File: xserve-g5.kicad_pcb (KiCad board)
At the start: 2 copper layers, 100 x 50 mm, 4 parts, among them J1 SATA_Backplane_PWR, J2 FAN_LEFT, J3 FAN_RIGHT, J4 PWR

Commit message: update
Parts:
- added J10: FAN5_PWM, Connector_PinSocket_2.54mm:PinSocket_1x04_P2.54mm_Horizontal, F.Cu at (191.0, 107.5)
- added J11: FAN6_PWM, Connector_PinSocket_2.54mm:PinSocket_1x04_P2.54mm_Horizontal, F.Cu at (169.5, 107.5)
- added J12: FAN7_PWM, Connector_PinSocket_2.54mm:PinSocket_1x04_P2.54mm_Horizontal, F.Cu at (148.0, 107.5)
- added J5: PWR_R, Connector_TE-Connectivity:TE_MATE-N-LOK_350211-1_1x04_P5.08mm_Vertical, F.Cu at (217.0, 110.0)
- added J6: FAN1_PWM, Connector_PinSocket_2.54mm:PinSocket_1x04_P2.54mm_Horizontal, F.Cu at (133.0, 107.5)
- added J7: FAN2_PWM, Connector_PinSocket_2.54mm:PinSocket_1x04_P2.54mm_Horizontal, F.Cu at (111.5, 107.5)
- added J8: FAN3_PWM, Connector_PinSocket_2.54mm:PinSocket_1x04_P2.54mm_Horizontal, F.Cu at (90.0, 107.5)
- added J9: FAN4_PWM, Connector_PinSocket_2.54mm:PinSocket_1x04_P2.54mm_Horizontal, F.Cu at (68.5, 107.5)
- added JP1: PWM1_2, Connector_PinHeader_2.54mm:PinHeader_1x02_P2.54mm_Vertical, F.Cu at (125.0, 101.0)
- added JP2: PWM1_3, Connector_PinHeader_2.54mm:PinHeader_1x02_P2.54mm_Vertical, F.Cu at (104.0, 101.0)
- added JP3: PWM1_4, Connector_PinHeader_2.54mm:PinHeader_1x02_P2.54mm_Vertical, F.Cu at (82.0, 101.0)
- added JP4: PWM5_6, Connector_PinHeader_2.54mm:PinHeader_1x02_P2.54mm_Vertical, F.Cu at (183.0, 101.0)
- added JP5: PWM5_7, Connector_PinHeader_2.54mm:PinHeader_1x02_P2.54mm_Vertical, F.Cu at (161.5, 101.0)
- J4: value PWR -> PWR_L
- moved J3 68.3 mm to (228.5, 79.5), turned to 90 degrees
- moved J1 67.9 mm to (33.5, 92.5)
- moved J2 65.8 mm to (59.5, 66.5)
- moved J4 65.2 mm to (36.0, 110.5)
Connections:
- J1 pad 8: +3V3 -> Net-(J1-Pad8)
- J1 pad 9: +3V3 -> Net-(J1-Pad9)
- J2 pad 1: Net-(J2-Pad1) -> PWM1
- J2 pad 10: Net-(J2-Pad10) -> TACH4
- J2 pad 2: Net-(J2-Pad2) -> PWM2
- J2 pad 3: Net-(J2-Pad3) -> GND
- J2 pad 4: Net-(J2-Pad4) -> PWM3
- J2 pad 5: Net-(J2-Pad5) -> PWM4
- J2 pad 6: Net-(J2-Pad6) -> TACH1
- J2 pad 7: Net-(J2-Pad7) -> TACH2
- J2 pad 8: Net-(J2-Pad8) -> +12V
- J2 pad 9: Net-(J2-Pad9) -> TACH3
- J3 pad 1: Net-(J3-Pad1) -> PWM5
- J3 pad 10: Net-(J3-Pad10) -> +12V
- J3 pad 2: Net-(J3-Pad2) -> PWM6
- J3 pad 3: Net-(J3-Pad3) -> GND
- J3 pad 4: Net-(J3-Pad4) -> PWM7
- J3 pad 5: Net-(J3-Pad5) -> GND
- J3 pad 6: Net-(J3-Pad6) -> TACH5
- J3 pad 7: Net-(J3-Pad7) -> TACH6
- J3 pad 8: Net-(J3-Pad8) -> +12V
- J3 pad 9: Net-(J3-Pad9) -> TACH7
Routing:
- net PWM1: track 0.00 -> 163.8 mm
- net TACH1: track 0.00 -> 103.0 mm
- net TACH7: track 0.00 -> 99.4 mm
- net PWM7: track 0.00 -> 88.6 mm
- net PWM2: track 0.00 -> 86.9 mm
- net PWM5: track 0.00 -> 85.2 mm
- net +12V: track 24.0 -> 105.3 mm
- net TACH2: track 0.00 -> 79.9 mm
- net TACH6: track 0.00 -> 75.4 mm
- net PWM6: track 0.00 -> 64.6 mm
- net PWM3: track 0.00 -> 62.2 mm
- net TACH3: track 0.00 -> 54.6 mm
- net TACH5: track 0.00 -> 52.7 mm
- net PWM4: track 0.00 -> 44.3 mm
- net TACH4: track 0.00 -> 36.1 mm
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- added copper zone on B.Cu, net GND
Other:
- board size 100 x 50 mm -> 214 x 56.5 mm
- net class GND added: clearance 0.2, trace_width 1, via_dia 0.8, via_drill 0.4
- net class PWM added: clearance 0.2, trace_width 0.5, via_dia 0.8, via_drill 0.4
- net class TACH added: clearance 0.2, trace_width 0.5, via_dia 0.8, via_drill 0.4

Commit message: update
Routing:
- net PWM5: track 85.2 -> 91.4 mm
- net TACH5: track 52.7 -> 47.0 mm
- net PWM1: track 163.8 -> 159.2 mm
- net TACH1: track 103.0 -> 98.6 mm
- net TACH6: track 75.4 -> 71.3 mm
- net TACH2: track 79.9 -> 75.8 mm
- net TACH7: track 99.4 -> 95.5 mm
- net PWM3: track 62.2 -> 66.0 mm
- net TACH3: track 54.6 -> 51.8 mm
- net PWM2: track 86.9 -> 89.0 mm
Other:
- outline, holes or cut-outs redrawn
- net class Default: clearance 0.2 -> 0.3
- net class GND: clearance 0.2 -> 0.3
- net class PWM: clearance 0.2 -> 0.3
- net class TACH: clearance 0.2 -> 0.3
- rule trace_clearance: 0.2 -> 0.3

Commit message: updates
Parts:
- added J13: Front Panel, Connector_PinHeader_1.27mm:PinHeader_2x17_P1.27mm_Vertical, F.Cu at (85.0, 71.5)
- added U1: WeMos_D1_mini, Module:WEMOS_D1_mini_light, F.Cu at (173.5, 85.0)
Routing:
- net PWM3: track 66.0 -> 62.3 mm
- net PWM1: track 159.2 -> 161.9 mm
- net TACH1: track 98.6 -> 101.0 mm
- net TACH2: track 75.8 -> 77.7 mm
- net PWM2: track 89.0 -> 88.2 mm
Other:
- outline, holes or cut-outs redrawn
- net class Default: clearance 0.3 -> 0.25
- net class GND: clearance 0.3 -> 0.25
- rule trace_clearance: 0.3 -> 0.25

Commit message: update
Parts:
- added J14: SYSTEM_PINS, Connector_PinHeader_2.54mm:PinHeader_1x06_P2.54mm_Horizontal, F.Cu at (102.5, 75.0)
- added J15: CLED_VCC, Connector_PinHeader_2.54mm:PinHeader_1x03_P2.54mm_Vertical, F.Cu at (123.0, 67.0)
- moved J13 4.74 mm to (86.5, 67.0)
- moved U1 3.91 mm to (176.5, 87.5)
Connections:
- net Net-(J13-Pad22) renamed Q13
- J13 pad 14: Net-(J13-Pad14) -> CLED_SRCLR_n
- J13 pad 20: U6_?? -> CLED_SRCLR_n
- J13 pad 26: +5V -> +5VA
- J13 pad 28: +5V -> +5VA
- J13 pad 30: +5V -> +5VA
- J13 pad 32: +5V -> +5VA
- J13 pad 34: +5V -> +5VA
- J13 pad 4: CLED_VCC -> CLED_SRCLR_n
- J13 pad 9: Net-(J13-Pad9) -> CLED_SRCLR_n
- J3 pad 10: +12V -> +12VA
- J3 pad 8: +12V -> +12VA
- J5 pad 1: +12V -> +12VA
- U1 pad 4: Net-(U1-Pad4) -> CLED_SRCLK
- U1 pad 5: Net-(U1-Pad5) -> CLED_SER
- U1 pad 6: Net-(U1-Pad6) -> CLED_RCLK
- U1 pad 9: +5V -> +5VA
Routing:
- net CLED_SRCLK: track 0.00 -> 110.2 mm, vias 0 -> 2
- net CLED_RCLK: track 0.00 -> 110.2 mm
- net CLED_SER: track 0.00 -> 105.8 mm
- net +5VA: track 0.00 -> 97.6 mm, vias 0 -> 2
- net +3V3: track 0.00 -> 87.5 mm, vias 0 -> 2
- net +12VA: track 0.00 -> 55.4 mm
- net +12V: track 104.9 -> 49.4 mm
- net CLED_SRCLR_n: track 0.00 -> 45.6 mm
- net GND: track 0.00 -> 32.0 mm, vias 0 -> 3
- net LANB_LED: track 0.00 -> 28.0 mm, vias 0 -> 1
- net SRVID_SW: track 0.00 -> 23.6 mm
- net PWR_LED: track 0.00 -> 18.2 mm
- net PWR_SW: track 0.00 -> 16.8 mm
- net LANA_LED: track 0.00 -> 11.5 mm
- net PWM1: track 161.9 -> 172.7 mm
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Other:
- outline, holes or cut-outs redrawn
- net class 3.3V: clearance 0.5 -> 0.25; trace_width 2 -> 0.5
- net class 5VA added: clearance 0.25, trace_width 0.5, via_dia 0.8, via_drill 0.4
- board text added: "BP"
- board text added: "CLED VCC 3.3 - 5"
- board text added: "FAN"
- board text added: "FAN1"
- board text added: "FAN1 PWM Passthrough"
- board text added: "FAN2"
- board text added: "FAN3"
- board text added: "FAN4"
- board text added: "FAN5"
- board text added: "FAN5 PWM Passthrough"
- board text added: "FAN6"
- board text added: "FAN7"
- board text added: "FP"
- board text added: "LANB LED LANA LED ID SW ID LED PWR SW PWR LED"
- board text added: "SER - GPIO12 - D6 RCLK - GPIO13 - D7 SRCLK - GPIO14 - D5"
- board text added: "Xserve G5 BP / FAN Left Adapter v1.0 envy/xserveg5-adapters"
- board text added: "Xserve G5 FAN Right Adapter v1.0 envy/xserveg5-adapters"
- board text added: "Xserve G5 FP Adapter v1.0 envy/xserveg5-adapters"

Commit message: update
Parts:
- added J16: CLED, Connector_PinHeader_2.54mm:PinHeader_1x05_P2.54mm_Horizontal, F.Cu at (133.5, 79.0)
- added J17: BP_SMBUS, Connector_PinHeader_2.54mm:PinHeader_1x05_P2.54mm_Horizontal, F.Cu at (43.5, 65.5)
- added JP6: PWM1_4, Connector_PinHeader_2.54mm:PinHeader_1x02_P2.54mm_Vertical, F.Cu at (125.5, 73.0)
- J14: footprint Connector_PinHeader_2.54mm:PinHeader_1x06_P2.54mm_Horizontal -> Connector_PinHeader_2.54mm:PinHeader_1x07_P2.54mm_Horizontal
- moved J14 4.00 mm to (102.5, 79.0)
- moved JP2 3.04 mm to (103.5, 104.0)
- moved JP1 3.00 mm to (125.0, 104.0)
- moved JP3 3.00 mm to (82.0, 104.0)
- moved JP4 3.00 mm to (183.0, 104.0)
- moved JP5 3.00 mm to (161.5, 104.0)
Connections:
- J1 pad 1: Net-(J1-Pad1) -> SMBUS_SCL
- J1 pad 7: Net-(J1-Pad7) -> SMBUS_SDA
- J1 pad 8: Net-(J1-Pad8) -> BP_UNKN
- J1 pad 9: Net-(J1-Pad9) -> SMBUS_VCC
- J13 pad 14: CLED_SRCLR_n -> CLED_VCC
- J13 pad 20: CLED_SRCLR_n -> CLED_VCC
- J13 pad 4: CLED_SRCLR_n -> CLED_VCC
- J13 pad 9: CLED_SRCLR_n -> CLED_VCC
- J15 pad 2: CLED_SRCLR_n -> CLED_VCC
- JP2 pad 2: PWM1 -> PWM2
- JP3 pad 2: PWM1 -> PWM3
- JP5 pad 2: PWM5 -> PWM6
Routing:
- net CLED_VCC: track 0.00 -> 75.2 mm, vias 0 -> 2
- net PWM1: track 172.7 -> 126.2 mm
- net PWM5: track 91.4 -> 56.0 mm
- net SMBUS_SDA: track 0.00 -> 32.1 mm
- net BP_UNKN: track 0.00 -> 31.3 mm
- net SMBUS_VCC: track 0.00 -> 30.6 mm
- net SMBUS_SCL: track 0.00 -> 29.0 mm
- net CLED_RCLK: track 110.2 -> 138.7 mm, vias 0 -> 1
- net CLED_SER: track 105.8 -> 128.3 mm, vias 0 -> 1
- net CLED_SRCLK: track 110.2 -> 131.5 mm
- net PWM6: track 64.6 -> 78.8 mm
- net PWM2: track 98.8 -> 110.2 mm
- net PWM3: track 73.1 -> 84.0 mm
- net SRVID_SW: track 23.6 -> 28.8 mm
- net LANB_LED: track 28.0 -> 33.1 mm
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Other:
- outline, holes or cut-outs redrawn
- board text added: "??? SDA SCL VCC GND"
- board text added: "FAN2 PWM Passthrough"
- board text added: "FAN3 PWM Passthrough"
- board text added: "FAN6 PWM Passthrough"
- board text added: "GND LANB LED LANA LED ID SW ID LED PWR SW PWR LED"
- board text added: "RCLK"
- board text added: "SER"
- board text added: "SER RCLK SRCLK SRCLR_n VCC"
- board text added: "SRCLK"
- board text added: "SRCLR - VCC"
- board text removed: "LANB LED LANA LED ID SW ID LED PWR SW PWR LED"

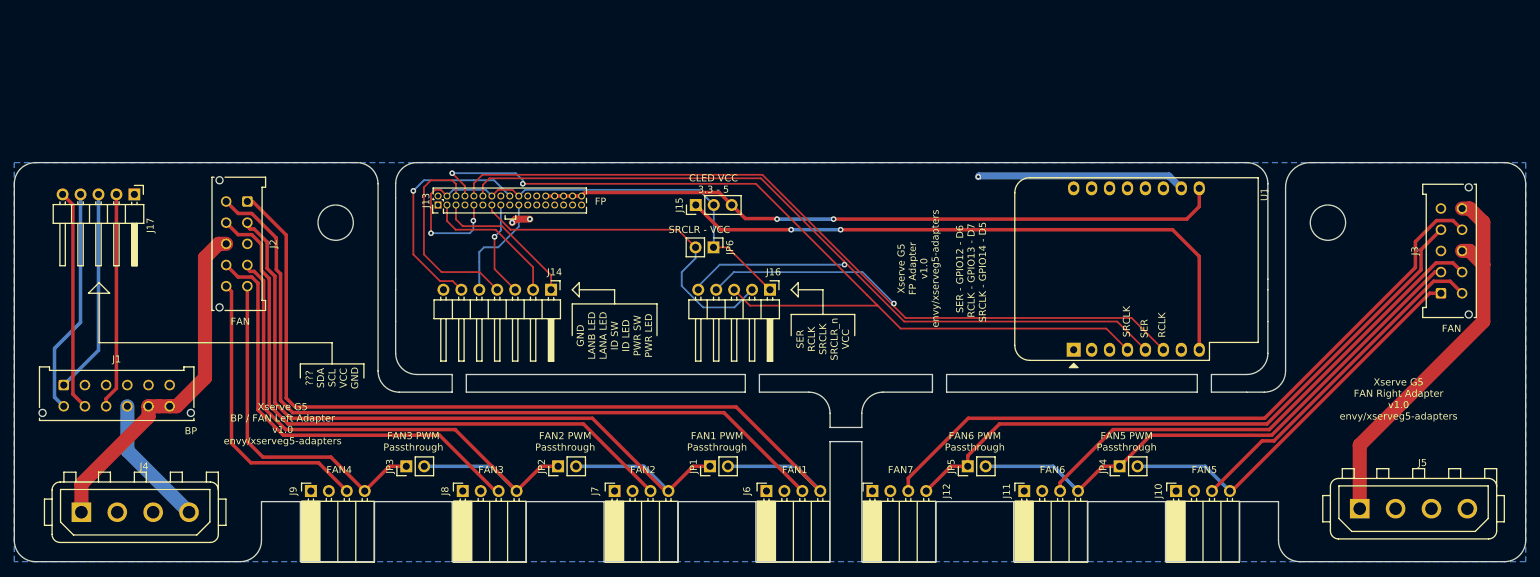
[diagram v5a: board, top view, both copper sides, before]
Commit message: Switch pwm and tacho pins...
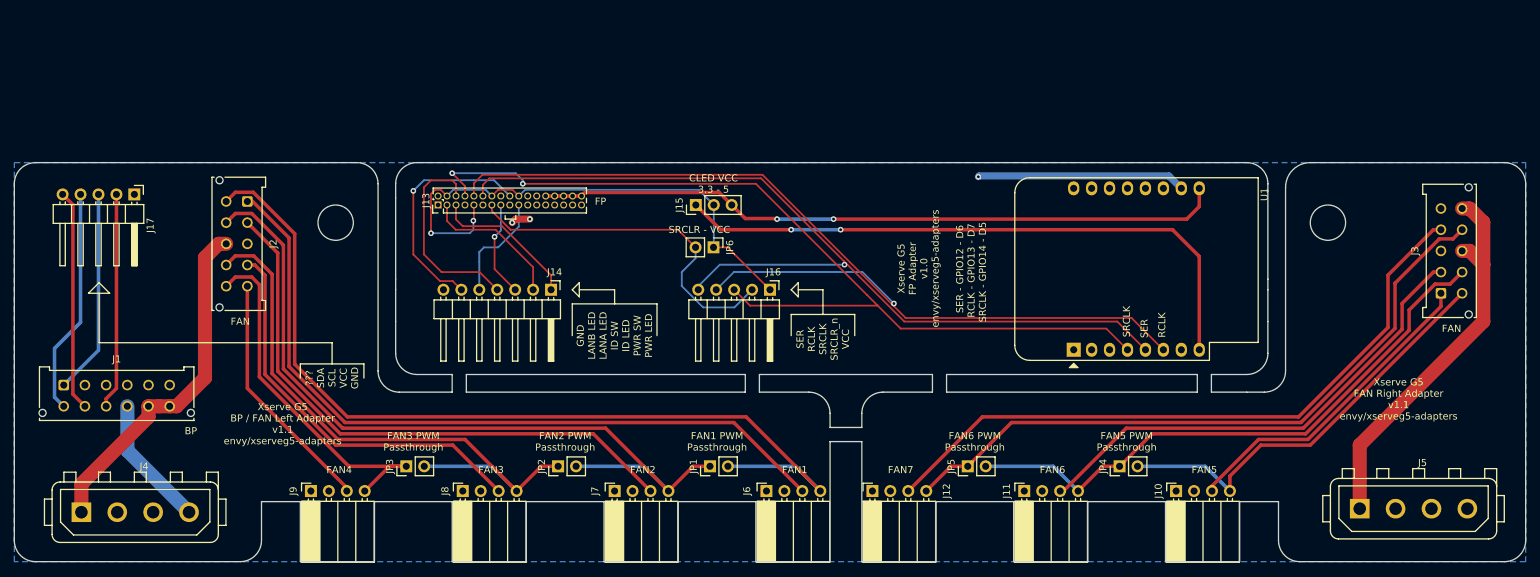
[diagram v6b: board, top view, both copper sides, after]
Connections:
- J2 pad 1: PWM1 -> TACH1
- J2 pad 10: TACH4 -> PWM4
- J2 pad 2: PWM2 -> TACH2
- J2 pad 4: PWM3 -> TACH3
- J2 pad 5: PWM4 -> TACH4
- J2 pad 6: TACH1 -> PWM1
- J2 pad 7: TACH2 -> PWM2
- J2 pad 9: TACH3 -> PWM3
- J3 pad 1: PWM5 -> TACH5
- J3 pad 2: PWM6 -> TACH6
- J3 pad 4: PWM7 -> TACH7
- J3 pad 6: TACH5 -> PWM5
- J3 pad 7: TACH6 -> PWM6
- J3 pad 9: TACH7 -> PWM7
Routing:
- net TACH4: track 41.7 -> 34.8 mm
- net TACH2: track 88.5 -> 82.6 mm
- net TACH1: track 111.7 -> 106.2 mm
- net TACH3: track 62.3 -> 57.1 mm
- net PWM6: track 78.8 -> 83.4 mm
- net PWM5: track 56.0 -> 60.2 mm
- net PWM7: track 90.8 -> 95.0 mm
- net PWM4: track 48.8 -> 52.1 mm
- net TACH7: track 98.0 -> 95.1 mm
- net TACH5: track 48.4 -> 45.5 mm
- net TACH6: track 71.5 -> 68.9 mm
- net PWM3: track 84.0 -> 85.5 mm
- net PWM1: track 126.2 -> 127.5 mm
- net PWM2: track 110.2 -> 111.6 mm
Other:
- board text added: "Xserve G5 BP / FAN Left Adapter v1.1 envy/xserveg5-adapters"
- board text added: "Xserve G5 FAN Right Adapter v1.1 envy/xserveg5-adapters"
- board text removed: "Xserve G5 BP / FAN Left Adapter v1.0 envy/xserveg5-adapters"
- board text removed: "Xserve G5 FAN Right Adapter v1.0 envy/xserveg5-adapters"
